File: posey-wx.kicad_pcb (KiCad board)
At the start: 4 copper layers, 25.3 x 23.4 mm, 31 parts, among them J1 TC2050-IDC-NL, Y1 XTAL, Y2 XTAL

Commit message: w2310 µ380
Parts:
- removed µC1: uC BMD-350-A-R, posey:BMD-350-A-R
- added U1: BMD-380-A-R, posey:XCVR_BMD-380-A-R, F.Cu at (175.1, 139.2)
- REG1: value MLF-6_ML_MCH -> MIC5219-3.3YML-TR
- moved C9 5.17 mm to (170.3, 144.2), turned to 90 degrees
- moved C8 4.11 mm to (173.4, 144.2), turned to 90 degrees
- moved Y1 3.96 mm to (171.8, 144.0), turned to 180 degrees
- moved R11 2.42 mm to (175.4, 144.2), turned to -90 degrees
- moved R9 1.02 mm to (174.4, 144.2), turned to 90 degrees
- moved G*** 0.19 mm to (174.4, 147.0)
- moved G*** 0.19 mm to (173.0, 149.2)
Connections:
- net Net-(µC1A-P0-03) renamed VBAT_SENSE
- J1 pad 7: EXT_P0_12 -> EXT_P0_11
- J1 pad 9: EXT_P0_15 -> EXT_P0_14
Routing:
- net EXT_P0_14: track 0.00 -> 8.74 mm
- net EXT_P0_15: track 8.55 -> 0.00 mm
- net EXT_P0_12: track 6.32 -> 0.00 mm
- net EXT_P0_11: track 0.00 -> 5.79 mm
- net SPI_CS_IMU: track 19.4 -> 14.7 mm
- net VCC: track 56.3 -> 59.6 mm
- net I_CHG: track 21.8 -> 19.1 mm
- net VBAT: track 42.4 -> 44.6 mm, vias 2 -> 4
- net SDA/SPI_CIPO: track 18.7 -> 16.8 mm
- net VBAT_SENSE: track 4.23 -> 2.66 mm, vias 2 -> 0
- net IMU_nRESET: track 18.2 -> 16.9 mm
- net SPI_COPI: track 15.4 -> 14.3 mm
- net GND: track 27.7 -> 26.7 mm, vias 66 -> 71
- net Net-(U1-P0.00/XTAL1): track 2.88 -> 3.51 mm
- net SWO: track 11.2 -> 10.7 mm
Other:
- board text added: "P0.11"
- board text added: "P0.14"
- board text added: "Posey Watch w2310 µ380 Anthony Wertz"
- board text removed: "P0.12"
- board text removed: "P0.15"
- board text removed: "Posey Watch w2310 Anthony Wertz"

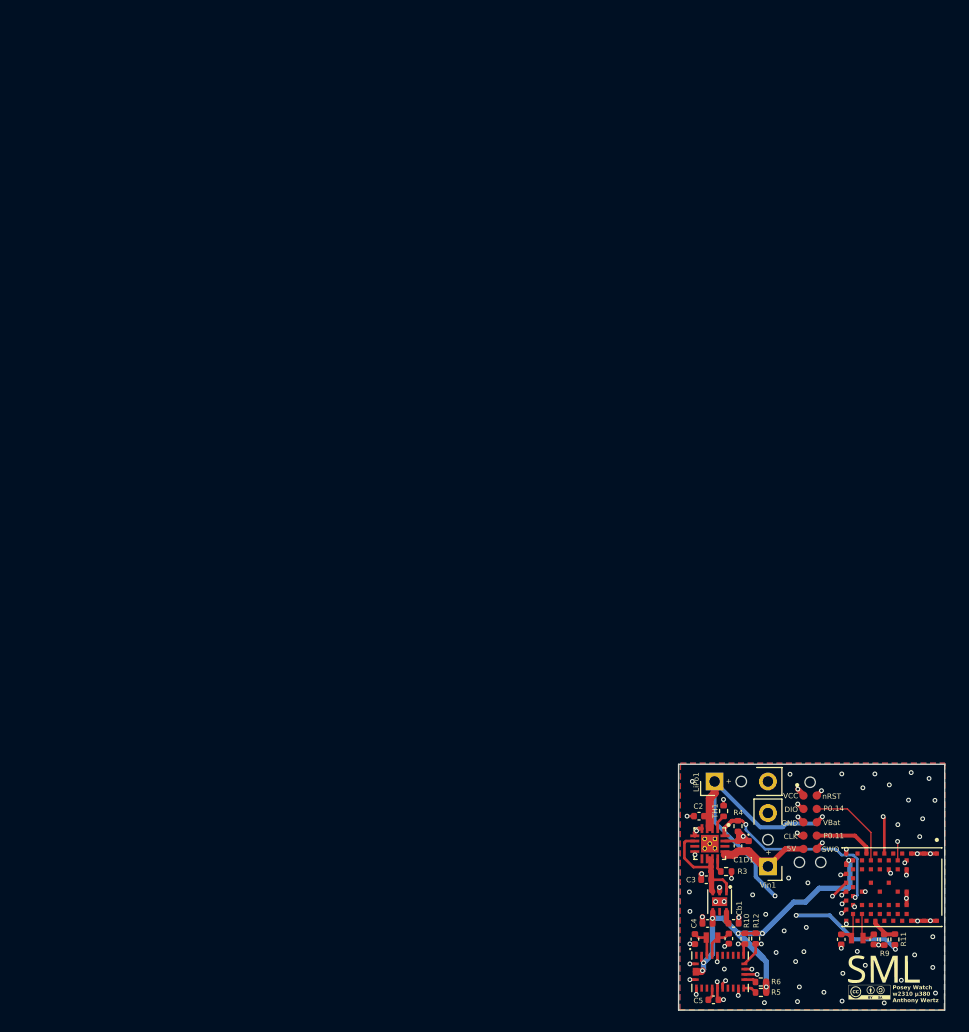
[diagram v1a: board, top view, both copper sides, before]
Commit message: Updated readme, license, and version.
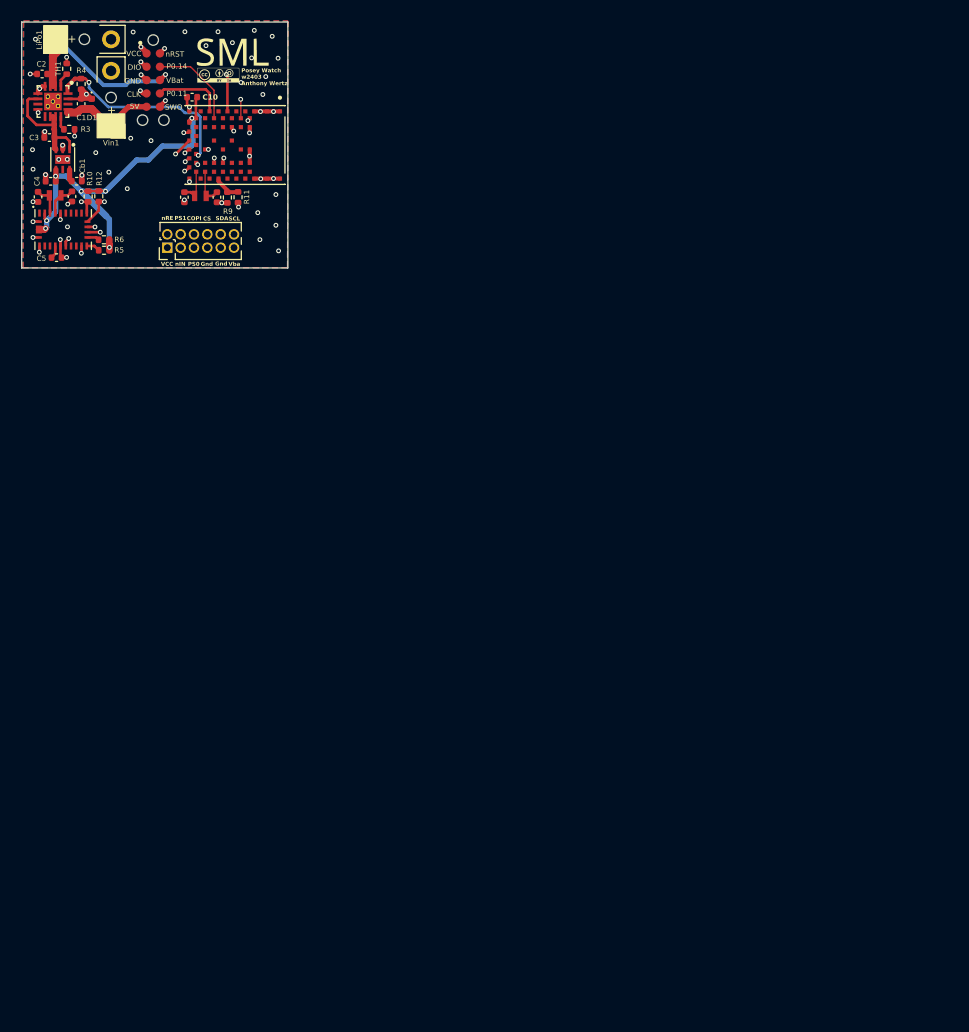
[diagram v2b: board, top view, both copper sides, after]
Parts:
- added C10: 0.1µ, Capacitor_SMD:C_0402_1005Metric, F.Cu at (108.5, 64.0)
- added J2: Conn_02x06_Odd_Even, Connector_PinHeader_1.27mm:PinHeader_2x06_P1.27mm_Vertical, F.Cu at (106.2, 78.3)
- IMU1: value BNO080 -> BNO086
- moved G*** 107.0 mm to (111.0, 61.9)
- moved G*** 107.0 mm to (112.4, 59.7)
- moved C1 94.3 mm to (98.0, 64.6)
- moved C2 94.3 mm to (94.3, 61.8)
- moved C3 94.3 mm to (94.9, 67.9)
- moved C4 94.3 mm to (95.1, 72.0)
- moved C5 94.3 mm to (95.6, 79.3)
- moved C7 94.3 mm to (97.1, 73.5)
- moved C8 94.3 mm to (110.9, 73.5)
- moved C9 94.3 mm to (107.8, 73.5)
- moved CHRG1 94.3 mm to (95.3, 64.4)
- moved Cb1 94.3 mm to (97.5, 72.0)
- moved IMU1 94.3 mm to (96.3, 76.6)
- moved J1 94.3 mm to (104.2, 59.8)
- moved R10 94.3 mm to (99.6, 73.4)
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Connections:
- IMU1 pad 5: GND -> IMU_PS1
- IMU1 pad 6: GND -> IMU_PS0
- U1 pad 42: unconnected-(U1-P0.30/AIN6-Pad42) -> IMU_PS1
- U1 pad 45: unconnected-(U1-P1.14-Pad45) -> IMU_PS0
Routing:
- net IMU_PS0: track 0.00 -> 38.8 mm, vias 0 -> 2
- net IMU_PS1: track 0.00 -> 36.7 mm, vias 0 -> 2
- net SDA/SPI_CIPO: track 16.8 -> 31.3 mm
- net SCL/SPI_SCK: track 15.0 -> 28.6 mm
- net SPI_CS_IMU: track 14.7 -> 26.4 mm
- net IMU_nINT: track 17.3 -> 28.5 mm
- net IMU_nRESET: track 16.9 -> 26.9 mm
- net SPI_COPI: track 14.3 -> 24.2 mm
- net VCC: track 59.6 -> 67.4 mm
- net VBAT: track 44.6 -> 49.8 mm, vias 4 -> 2
- net EXT_P0_11: track 5.79 -> 6.76 mm
- net GND: track 26.7 -> 26.5 mm, vias 71 -> 56
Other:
- copper layers 4 -> 6
- board text added: "COPI"
- board text added: "CS"
- board text added: "Gnd"
- board text added: "PS0"
- board text added: "PS1"
- board text added: "Posey Watch w2403 Anthony Wertz"
- board text added: "SCL"
- board text added: "SDA"
- board text added: "Vba"
- board text added: "nIN"
- board text added: "nRE"
- board text removed: "Posey Watch w2310 µ380 Anthony Wertz"
